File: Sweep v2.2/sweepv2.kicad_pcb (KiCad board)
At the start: 2 copper layers, 216.9 x 86.9 mm, 51 parts, among them J1 AudioJack4dpb, J2 AudioJack4dpb, SW10 SW_Push, SW11 SW_Push, SW11_r1 SW_Push, SW12 SW_Push, SW12_r1 SW_Push, SW13_r1 SW_Push, SW14 SW_Push, SW15 SW_Push, SW15_r1 SW_Push, SW16 SW_Push, SW16_r1 SW_Push, SW17 SW_Push, SW17_r1 SW_Push, SW18 SW_Push, SW18_r1 SW_Push, SW2 SW_Push, SW20 SW_Push, SW20_r1 SW_Push, SW21 SW_Push, SW21_r1 SW_Push, SW2_r1 SW_Push, SW3 SW_Push, SW3_r1 SW_Push, SW4 SW_Push, SW4_r1 SW_Push, SW5 SW_Push, SW5_r1 SW_Push, SW6 SW_Push, SW6_r1 SW_Push, SW7_r1 SW_Push, SW8 SW_Push, SW8_r1 SW_Push, SW9 SW_Push, SW9_r1 SW_Push, U1 ProMicro-kbd, U2 ProMicro-kbd

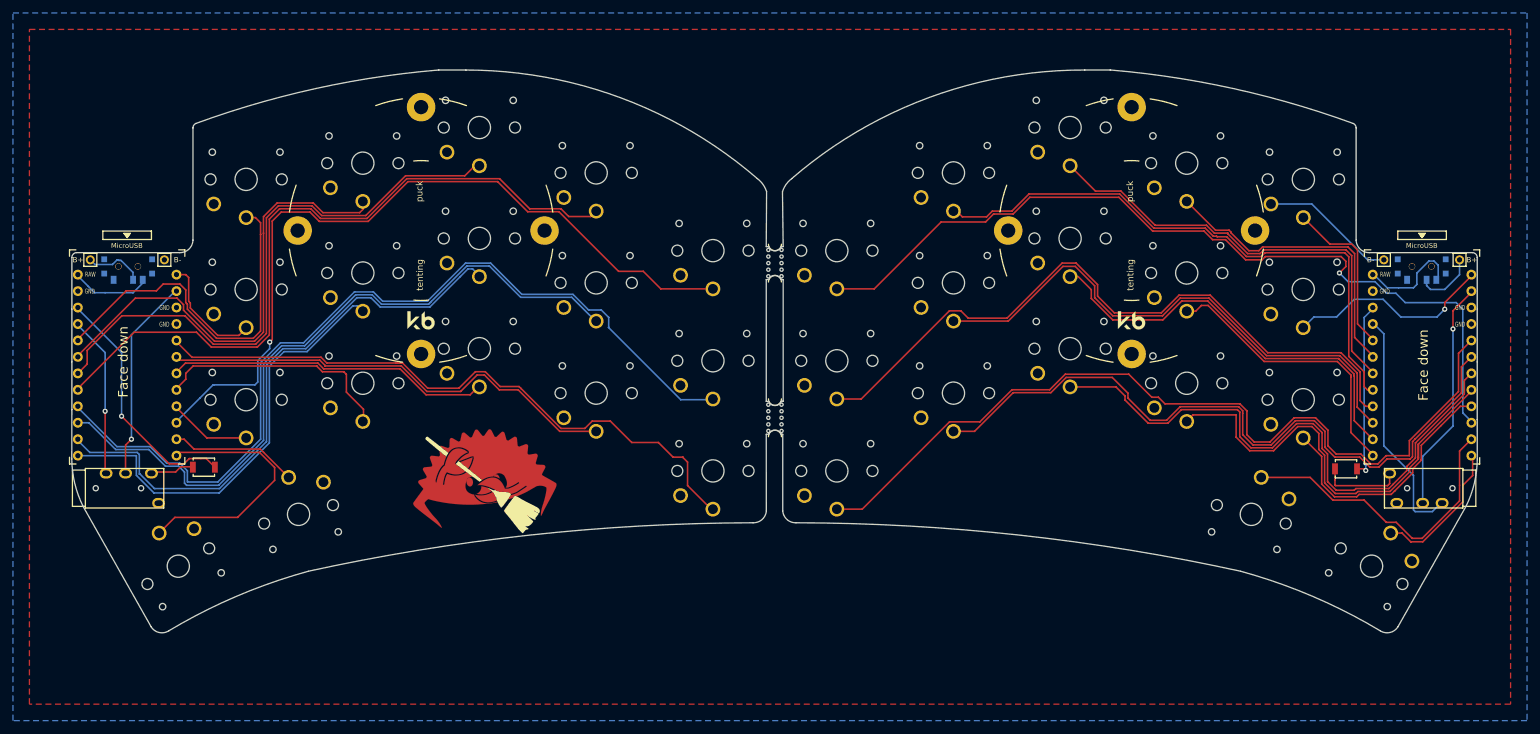
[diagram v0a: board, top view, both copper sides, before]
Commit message: Remove TRRS jacks
They are not used with ZMK.
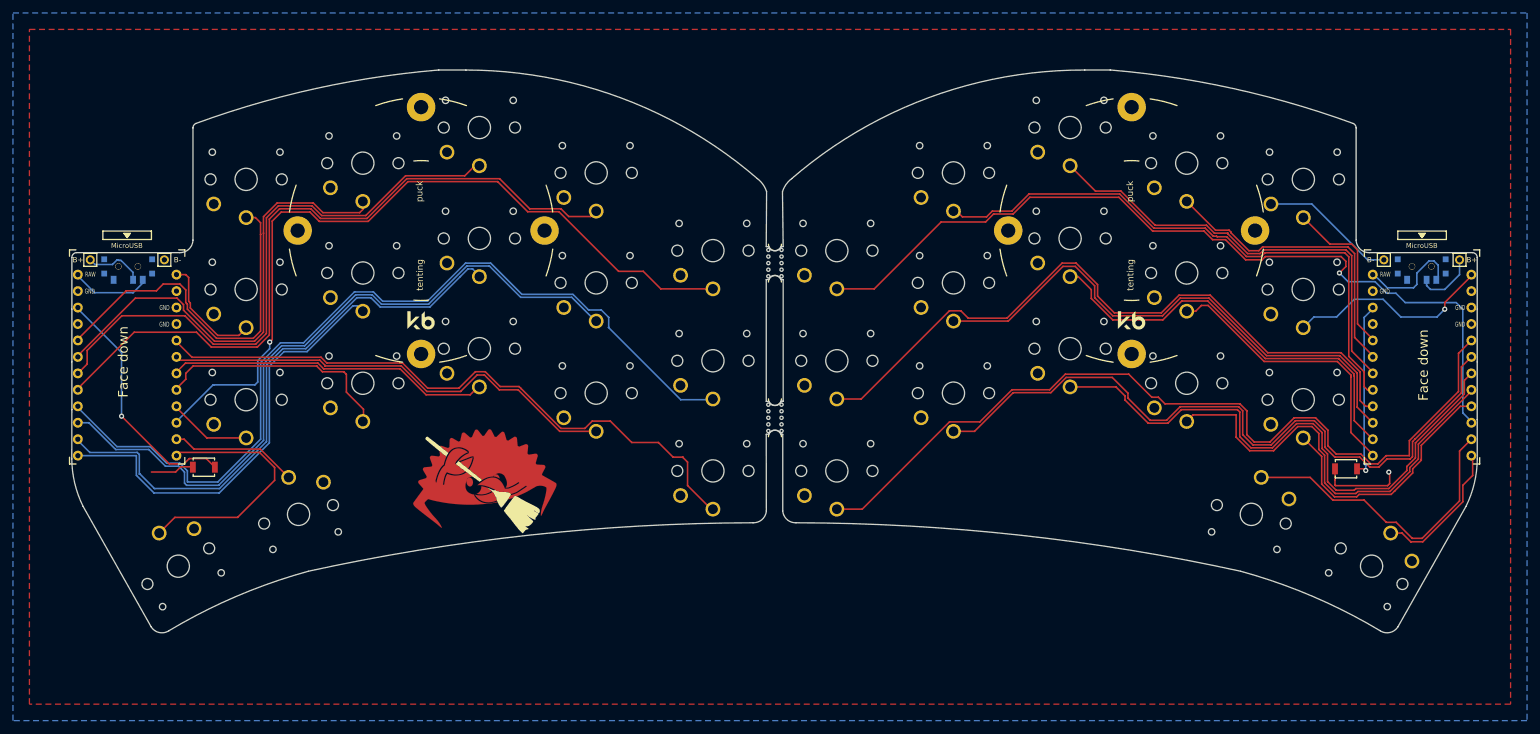
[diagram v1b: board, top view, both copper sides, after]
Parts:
- removed J1, J2: AudioJack4dpb, Kailh:TRRS-PJ-320A
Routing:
- net vcc: track 61.1 -> 0.00 mm, vias 1 -> 0
- net Switch18: track 35.7 -> 0.00 mm, vias 1 -> 0
- net Switch18_r: track 31.1 -> 0.00 mm, vias 1 -> 0
- net Switch14: track 69.3 -> 67.0 mm
- net Switch11_r: track 100.0 -> 99.4 mm
- net gnd: track 40.7 -> 40.6 mm, vias 0 -> 1

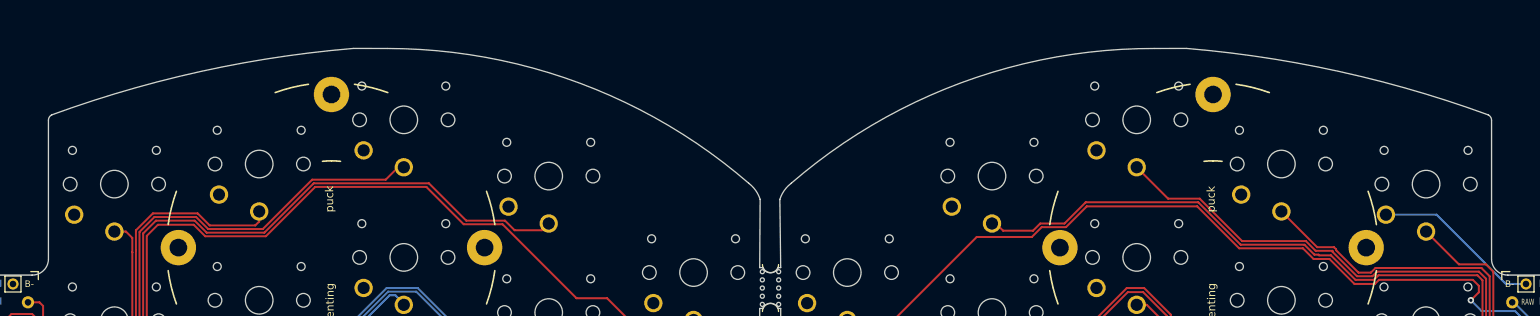
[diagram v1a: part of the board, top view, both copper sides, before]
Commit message: Update board outline a little bit
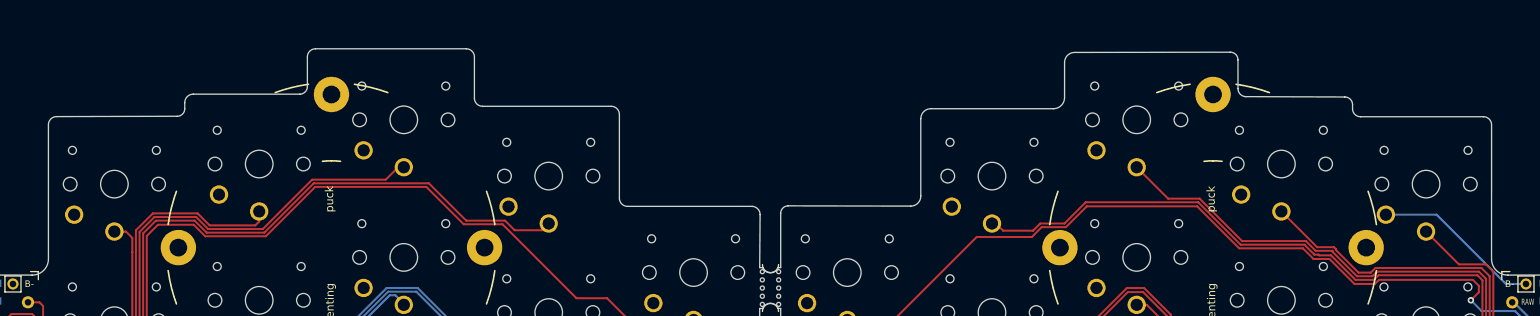
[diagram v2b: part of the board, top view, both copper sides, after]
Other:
- board size 216.9 x 86.9 mm -> 216.9 x 86.8 mm
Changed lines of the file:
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@@
   (gr_rect (start 226.822 50.419) (end 233.426 53.34) (layer "B.SilkS") (width 0.12) (fill none))
   (gr_line (start 131.5085 77.724) (end 131.506254 89.547024) (layer "Edge.Cuts") (width 0.05))
-  (gr_line (start 219.998001 47.763999) (end 219.998045 30.439419) (layer "Edge.Cuts") (width 0.05))
+  (gr_line (start 219.998001 47.763999) (end 220 31) (layer "Edge.Cuts") (width 0.05))
   (gr_arc (start 226.446 107.451265) (mid 225.204995 108.32098) (end 223.714 108.05) (layer "Edge.Cuts") (width 0.05))
   (gr_arc (start 222.033002 49.694917) (mid 220.620534 49.145716) (end 219.998001 47.763999) (layer "Edge.Cuts") (width 0.05))
-  (gr_arc (start 182.067777 21.502679) (mid 201.091879 24.375764) (end 219.56329 29.758889) (layer "Edge.Cuts") (width 0.05))
-  (gr_arc (start 132.893 38.265) (mid 153.988491 25.788882) (end 178.120389 21.508139) (layer "Edge.Cuts") (width 0.05))
   (gr_arc (start 237.938 49.692) (mid 238.46833 49.91167) (end 238.688 50.442) (layer "Edge.Cuts") (width 0.05))
-  (gr_arc (start 131.466055 40.278702) (mid 132.022929 39.160882) (end 132.893 38.265) (layer "Edge.Cuts") (width 0.05))
   (gr_arc (start 133.544 91.383119) (mid 132.156573 90.874102) (end 131.506254 89.547024) (layer "Edge.Cuts") (width 0.05))
-  (gr_arc (start 219.56329 29.758889) (mid 219.880079 30.035645) (end 219.998045 30.439419) (layer "Edge.Cuts") (width 0.05))
   (gr_arc (start 202.185134 98.863946) (mid 213.262488 102.723597) (end 223.714 108.05) (layer "Edge.Cuts") (width 0.05))
   (gr_line (start 222.033002 49.694917) (end 237.938 49.692) (layer "Edge.Cuts") (width 0.05))
@@
   (gr_line (start 236.953304 88.85815) (end 226.446 107.451265) (layer "Edge.Cuts") (width 0.05))
   (gr_arc (start 238.7 81.534) (mid 238.242913 85.295347) (end 236.953304 88.85815) (layer "Edge.Cuts") (width 0.05))
-  (gr_line (start 182.067777 21.502679) (end 178.120389 21.508139) (layer "Edge.Cuts") (width 0.05))
   (gr_line (start 238.688 50.442) (end 238.688 58.42) (layer "Edge.Cuts") (width 0.05))
-  (gr_line (start 131.466055 40.278702) (end 131.572 48.768) (layer "Edge.Cuts") (width 0.05))
+  (gr_line (start 131.57265 42.013084) (end 131.572 48.768) (layer "Edge.Cuts") (width 0.05))
   (gr_line (start 129.3495 48.768) (end 128.96 48.768) (layer "Edge.Cuts") (width 0.05))
   (gr_line (start 238.688 66.548) (end 238.688 75.438) (layer "Edge.Cuts") (width 0.05))
@@
   (gr_line (start 129.3495 77.724) (end 128.96 77.724) (layer "Edge.Cuts") (width 0.05))
   (gr_line (start 131.572 53.848) (end 131.572 72.644) (layer "Edge.Cuts") (width 0.05))
-  (gr_line (start 78.412223 21.502679) (end 82.613611 21.508139) (layer "Edge.Cuts") (width 0.05))
   (gr_line (start 21.792 50.442) (end 21.792 58.42) (layer "Edge.Cuts") (width 0.05))
   (gr_line (start 128.96 77.724) (end 128.975507 89.545022) (layer "Edge.Cuts") (width 0.05))
-  (gr_arc (start 127.587 38.265) (mid 128.457071 39.160882) (end 129.013945 40.278702) (layer "Edge.Cuts") (width 0.05))
   (gr_arc (start 128.975507 89.545022) (mid 128.324689 90.873432) (end 126.936 91.383119) (layer "Edge.Cuts") (width 0.05))
-  (gr_line (start 40.481999 47.763999) (end 40.481955 30.439419) (layer "Edge.Cuts") (width 0.05))
+  (gr_line (start 40.481999 47.763999) (end 40.481955 31) (layer "Edge.Cuts") (width 0.05))
   (gr_line (start 21.792 66.548) (end 21.792 73.914) (layer "Edge.Cuts") (width 0.05))
   (gr_line (start 23.526696 88.85815) (end 34.034 107.451265) (layer "Edge.Cuts") (width 0.05))
   (gr_arc (start 40.481999 47.763999) (mid 39.859467 49.145716) (end 38.446998 49.694917) (layer "Edge.Cuts") (width 0.05))
-  (gr_arc (start 40.91671 29.758889) (mid 59.388121 24.375764) (end 78.412223 21.502679) (layer "Edge.Cuts") (width 0.05))
   (gr_arc (start 58.294866 98.863946) (mid 92.415558 93.289555) (end 126.936 91.383119) (layer "Edge.Cuts") (width 0.05))
   (gr_arc (start 23.526696 88.85815) (mid 22.237087 85.295347) (end 21.78 81.534) (layer "Edge.Cuts") (width 0.05))
@@
   (gr_line (start 38.446998 49.694917) (end 22.542 49.692) (layer "Edge.Cuts") (width 0.05))
   (gr_line (start 21.792 58.42) (end 21.792 66.548) (layer "Edge.Cuts") (width 0.05))
-  (gr_arc (start 40.481955 30.439419) (mid 40.599921 30.035645) (end 40.91671 29.758889) (layer "Edge.Cuts") (width 0.05))
   (gr_arc (start 36.766 108.05) (mid 35.275005 108.32098) (end 34.034 107.451265) (layer "Edge.Cuts") (width 0.05))
-  (gr_arc (start 82.613611 21.508139) (mid 106.610476 25.833455) (end 127.587 38.265) (layer "Edge.Cuts") (width 0.05))
   (gr_arc (start 36.766 108.05) (mid 47.217512 102.723597) (end 58.294866 98.863946) (layer "Edge.Cuts") (width 0.05))
   (gr_line (start 21.792 73.914) (end 21.78 81.534) (layer "Edge.Cuts") (width 0.05))
   (gr_line (start 128.96 53.848) (end 128.96 72.644) (layer "Edge.Cuts") (width 0.05))
-  (gr_line (start 129.013945 40.278702) (end 128.96 48.768) (layer "Edge.Cuts") (width 0.05))
+  (gr_line (start 129.00875 42.164054) (end 128.96 48.768) (layer "Edge.Cuts") (width 0.05))
+  (gr_line (start 111.506 40.132) (end 111.506 29.718) (layer "Edge.Cuts") (width 0.05))
+  (gr_arc (start 201.75 27.542893) (mid 202.426777 27.823223) (end 202.707107 28.5) (layer "Edge.Cuts") (width 0.05))
+  (gr_arc (start 40.481955 31) (mid 40.780133 30.280133) (end 41.5 29.981955) (layer "Edge.Cuts") (width 0.05))
+  (gr_arc (start 92.456 21.54642) (mid 93.17442 21.844) (end 93.472 22.56242) (layer "Edge.Cuts") (width 0.05))
+  (gr_line (start 201.75 27.542893) (end 189.457107 27.5) (layer "Edge.Cuts") (width 0.05))
+  (gr_arc (start 72.69242 22.56242) (mid 72.99 21.844) (end 73.70842 21.54642) (layer "Edge.Cuts") (width 0.05))
+  (gr_arc (start 149 39.866117) (mid 148.633883 40.75) (end 147.75 41.116117) (layer "Edge.Cuts") (width 0.05))
+  (gr_line (start 188.457107 26.5) (end 188.453336 22.92411) (layer "Edge.Cuts") (width 0.05))
+  (gr_arc (start 149 30.25) (mid 149.366117 29.366117) (end 150.25 29) (layer "Edge.Cuts") (width 0.05))
+  (gr_arc (start 131.57265 42.013084) (mid 131.840282 41.361356) (end 132.488701 41.085803) (layer "Edge.Cuts") (width 0.05))
+  (gr_line (start 219 30) (end 203.707107 30) (layer "Edge.Cuts") (width 0.05))
   (gr_line (start 131.572 48.768) (end 131.2545 48.768) (layer "Edge.Cuts") (width 0.05))
+  (gr_arc (start 57.440242 28.247822) (mid 57.75 27.5) (end 58.497822 27.190242) (layer "Edge.Cuts") (width 0.05))
+  (gr_arc (start 112.522 41.148) (mid 111.80358 40.85042) (end 111.506 40.132) (layer "Edge.Cuts") (width 0.05))
+  (gr_arc (start 187.5 21.970774) (mid 188.17411 22.25) (end 188.453336 22.92411) (layer "Edge.Cuts") (width 0.05))
+  (gr_line (start 92.456 21.54642) (end 73.70842 21.54642) (layer "Edge.Cuts") (width 0.05))
+  (gr_line (start 110.49 28.702) (end 94.488 28.702) (layer "Edge.Cuts") (width 0.05))
   (gr_arc (start 131.254499 72.644) (mid 130.302 73.288873) (end 129.349501 72.643999) (layer "Edge.Cuts") (width 0.05))
   (gr_line (start 131.572 53.848) (end 131.2545 53.848) (layer "Edge.Cuts") (width 0.05))
+  (gr_line (start 165.5 29) (end 150.25 29) (layer "Edge.Cuts") (width 0.05))
+  (gr_arc (start 219 30) (mid 219.707107 30.292893) (end 220 31) (layer "Edge.Cuts") (width 0.05))
   (gr_arc (start 129.349501 77.724) (mid 130.302 77.079127) (end 131.254499 77.724001) (layer "Edge.Cuts") (width 0.05))
+  (gr_line (start 56.5 29.940242) (end 41.5 29.981955) (layer "Edge.Cuts") (width 0.05))
+  (gr_line (start 57.440242 28.247822) (end 57.440242 29) (layer "Edge.Cuts") (width 0.05))
+  (gr_arc (start 189.457107 27.5) (mid 188.75 27.207107) (end 188.457107 26.5) (layer "Edge.Cuts") (width 0.05))
+  (gr_line (start 166.883883 23.25) (end 166.882164 27.617836) (layer "Edge.Cuts") (width 0.05))
+  (gr_arc (start 94.488 28.702) (mid 93.76958 28.40442) (end 93.472 27.686) (layer "Edge.Cuts") (width 0.05))
+  (gr_line (start 202.707107 29) (end 202.707107 28.5) (layer "Edge.Cuts") (width 0.05))
+  (gr_line (start 147.75 41.116117) (end 132.488701 41.085803) (layer "Edge.Cuts") (width 0.05))
+  (gr_line (start 93.472 27.686) (end 93.472 22.56242) (layer "Edge.Cuts") (width 0.05))
+  (gr_line (start 149 30.25) (end 149 39.866117) (layer "Edge.Cuts") (width 0.05))
+  (gr_arc (start 110.49 28.702) (mid 111.20842 28.99958) (end 111.506 29.718) (layer "Edge.Cuts") (width 0.05))
+  (gr_line (start 128.016 41.148) (end 112.522 41.148) (layer "Edge.Cuts") (width 0.05))
+  (gr_arc (start 203.707107 30) (mid 203 29.707107) (end 202.707107 29) (layer "Edge.Cuts") (width 0.05))
+  (gr_arc (start 72.69242 26.25) (mid 72.416392 26.916392) (end 71.75 27.19242) (layer "Edge.Cuts") (width 0.05))
+  (gr_line (start 72.69242 22.56242) (end 72.69242 26.25) (layer "Edge.Cuts") (width 0.05))
+  (gr_arc (start 166.883883 23.25) (mid 167.25 22.366117) (end 168.133883 22) (layer "Edge.Cuts") (width 0.05))
+  (gr_arc (start 166.882164 27.617836) (mid 166.477338 28.595174) (end 165.5 29) (layer "Edge.Cuts") (width 0.05))
   (gr_line (start 131.572 72.644) (end 131.2545 72.644) (layer "Edge.Cuts") (width 0.05))
+  (gr_arc (start 57.440242 29) (mid 57.164851 29.664851) (end 56.5 29.940242) (layer "Edge.Cuts") (width 0.05))
   (gr_arc (start 131.254499 48.768) (mid 130.302 49.412873) (end 129.349501 48.767999) (layer "Edge.Cuts") (width 0.05))
   (gr_line (start 131.5085 77.724) (end 131.2545 77.724) (layer "Edge.Cuts") (width 0.05))
   (gr_arc (start 129.349501 53.848) (mid 130.302 53.203127) (end 131.254499 53.848001) (layer "Edge.Cuts") (width 0.05))
+  (gr_line (start 187.5 21.970774) (end 168.133883 22) (layer "Edge.Cuts") (width 0.05))
+  (gr_arc (start 128.016 41.148001) (mid 128.716307 41.456772) (end 129.00875 42.164054) (layer "Edge.Cuts") (width 0.05))
+  (gr_line (start 71.75 27.19242) (end 58.497822 27.190242) (layer "Edge.Cuts") (width 0.05))
   (gr_text "Sweep v 2.2" (at 140.97 39.116) (layer "B.SilkS")
     (effects (font (size 1.5 1.5) (thickness 0.3)) (justify mirror))

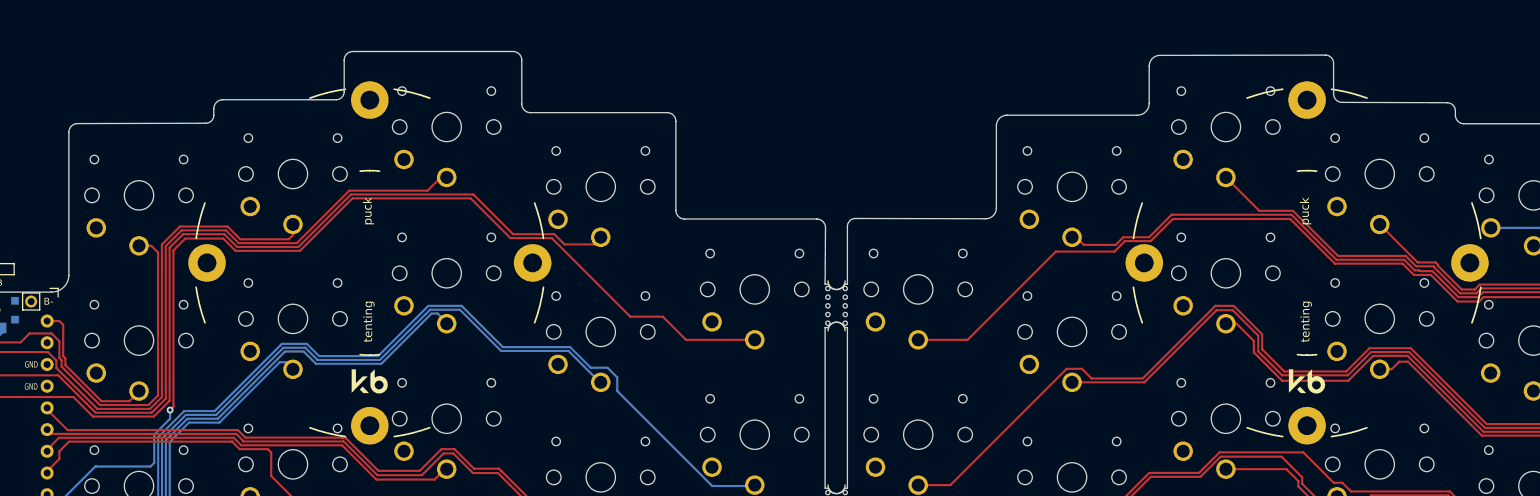
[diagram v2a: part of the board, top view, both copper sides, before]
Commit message: Remove the tilting puck holes and adjust the shape
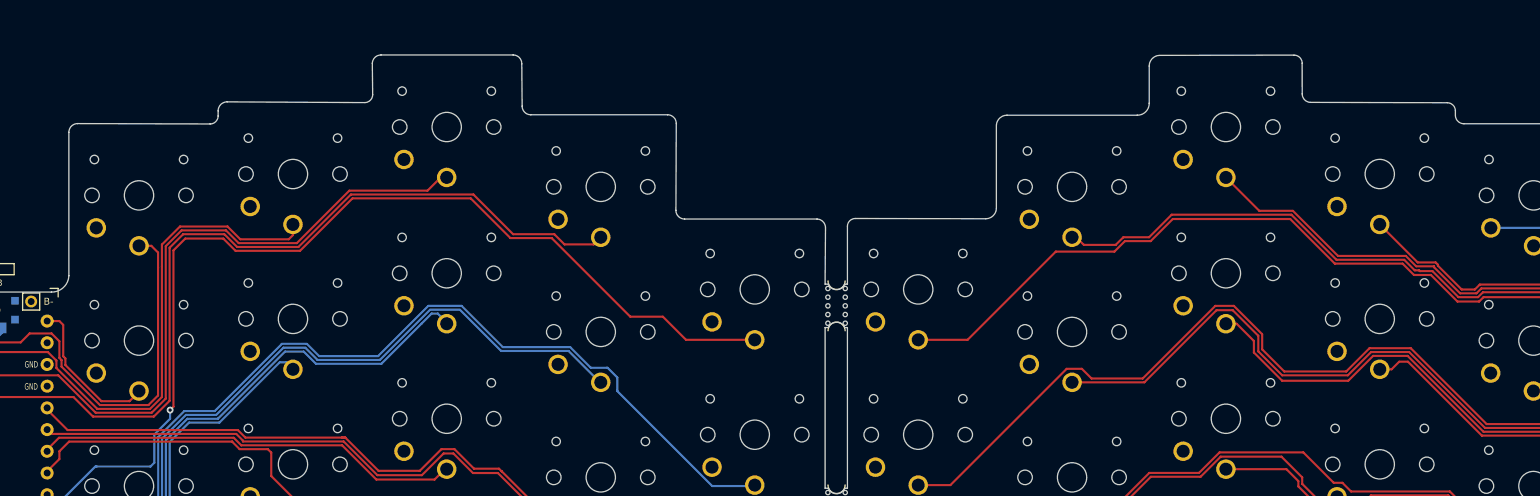
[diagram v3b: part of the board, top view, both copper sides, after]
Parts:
- removed REF** (x2): Tenting Puck, kbd:Tenting_Puck2
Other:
- board size 216.9 x 86.8 mm -> 216.9 x 86.4 mm
